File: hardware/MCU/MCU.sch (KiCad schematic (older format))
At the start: 4 parts

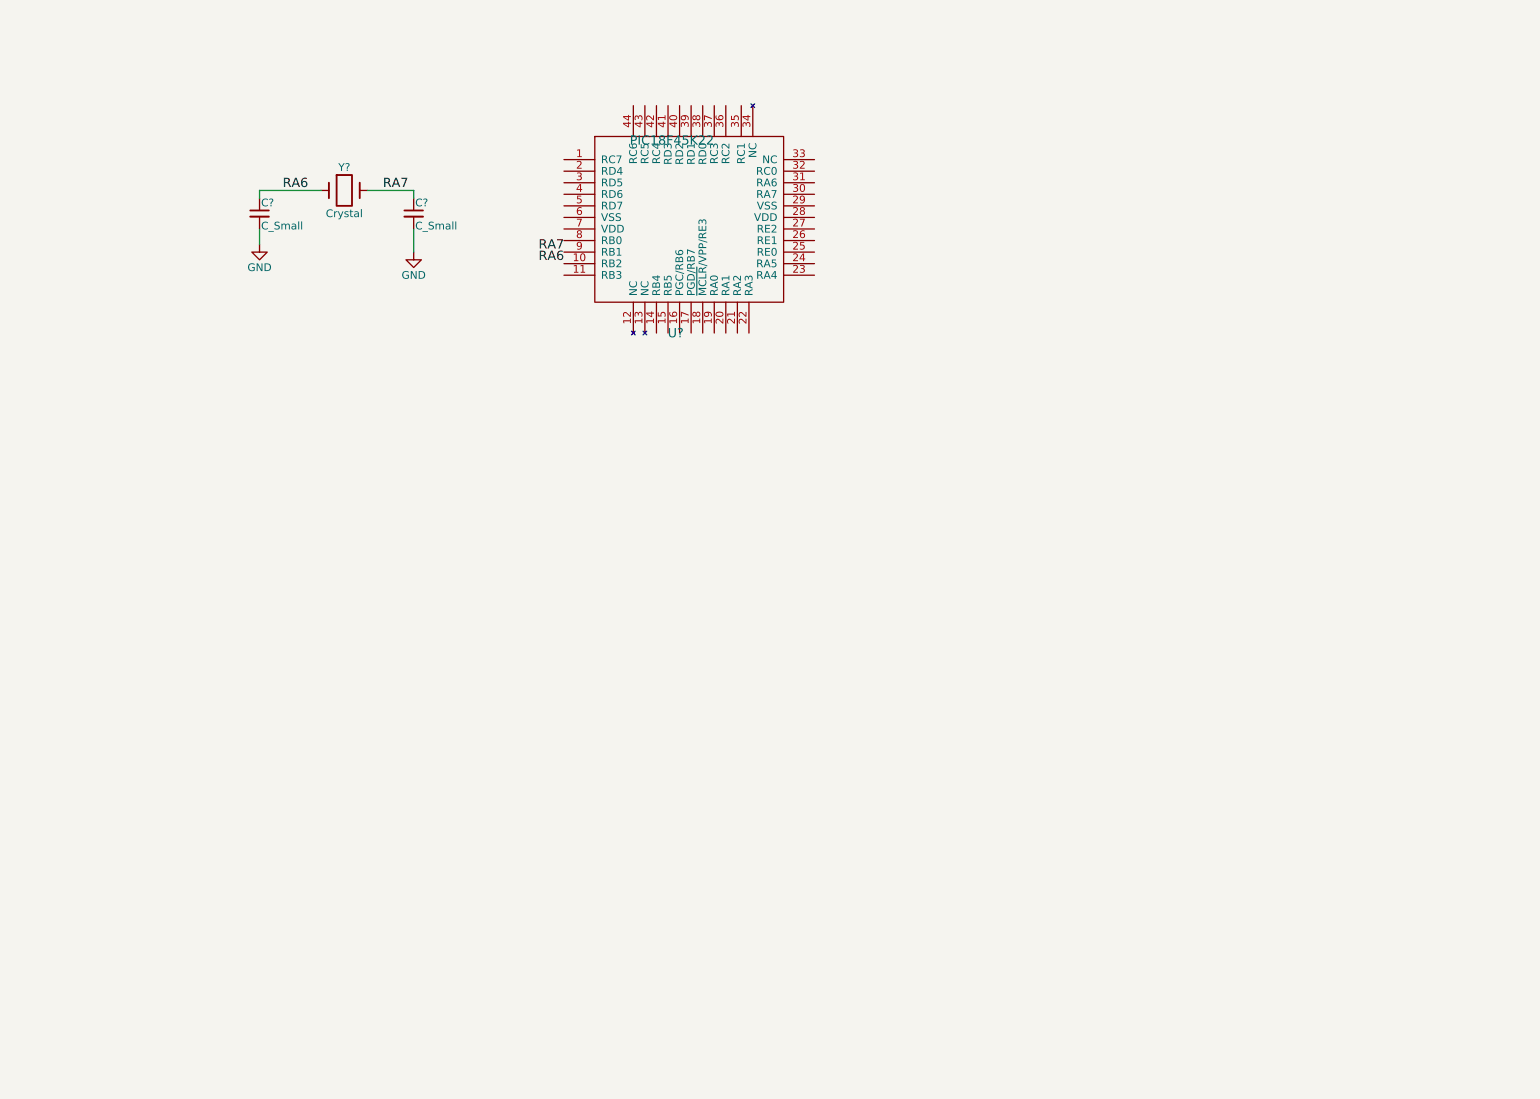
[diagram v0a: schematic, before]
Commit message: MCU: Connectors, watchdog, buzzer added
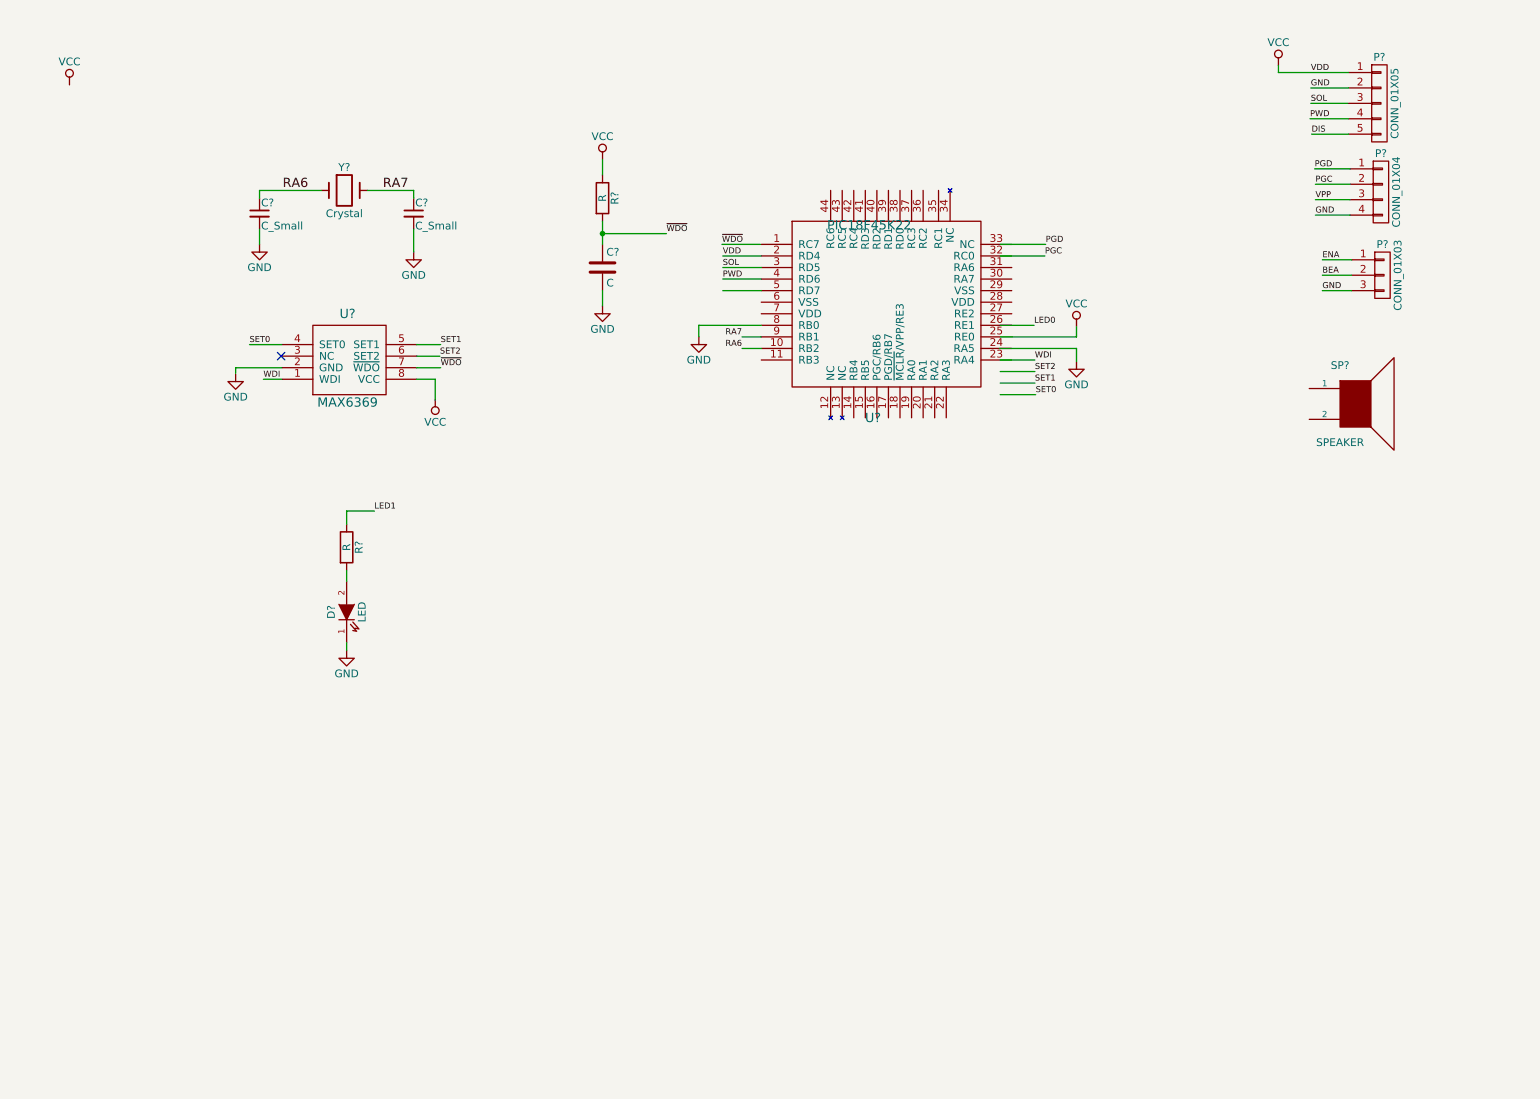
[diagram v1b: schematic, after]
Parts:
- added C?: C, symbol C
- added D?: LED, symbol LED
- added P?: CONN_01X04, symbol CONN_01X04
- added P?: CONN_01X03, symbol CONN_01X03
- added P?: CONN_01X05, symbol CONN_01X05
- added R? (x2): R, symbol R
- added SP?: SPEAKER, symbol SPEAKER
- added U?: MAX6369, symbol MAX6369
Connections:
- net labels added: BEA, DIS, ENA, LED0, LED1, PGC, PGD, PWD, SET0, SET1, SET2, SOL, VCC, VDD, VPP, WDI, ~WDO
- wire segments 6 -> 56
- no-connect marks 0 -> 1
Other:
- moved on the sheet: U?

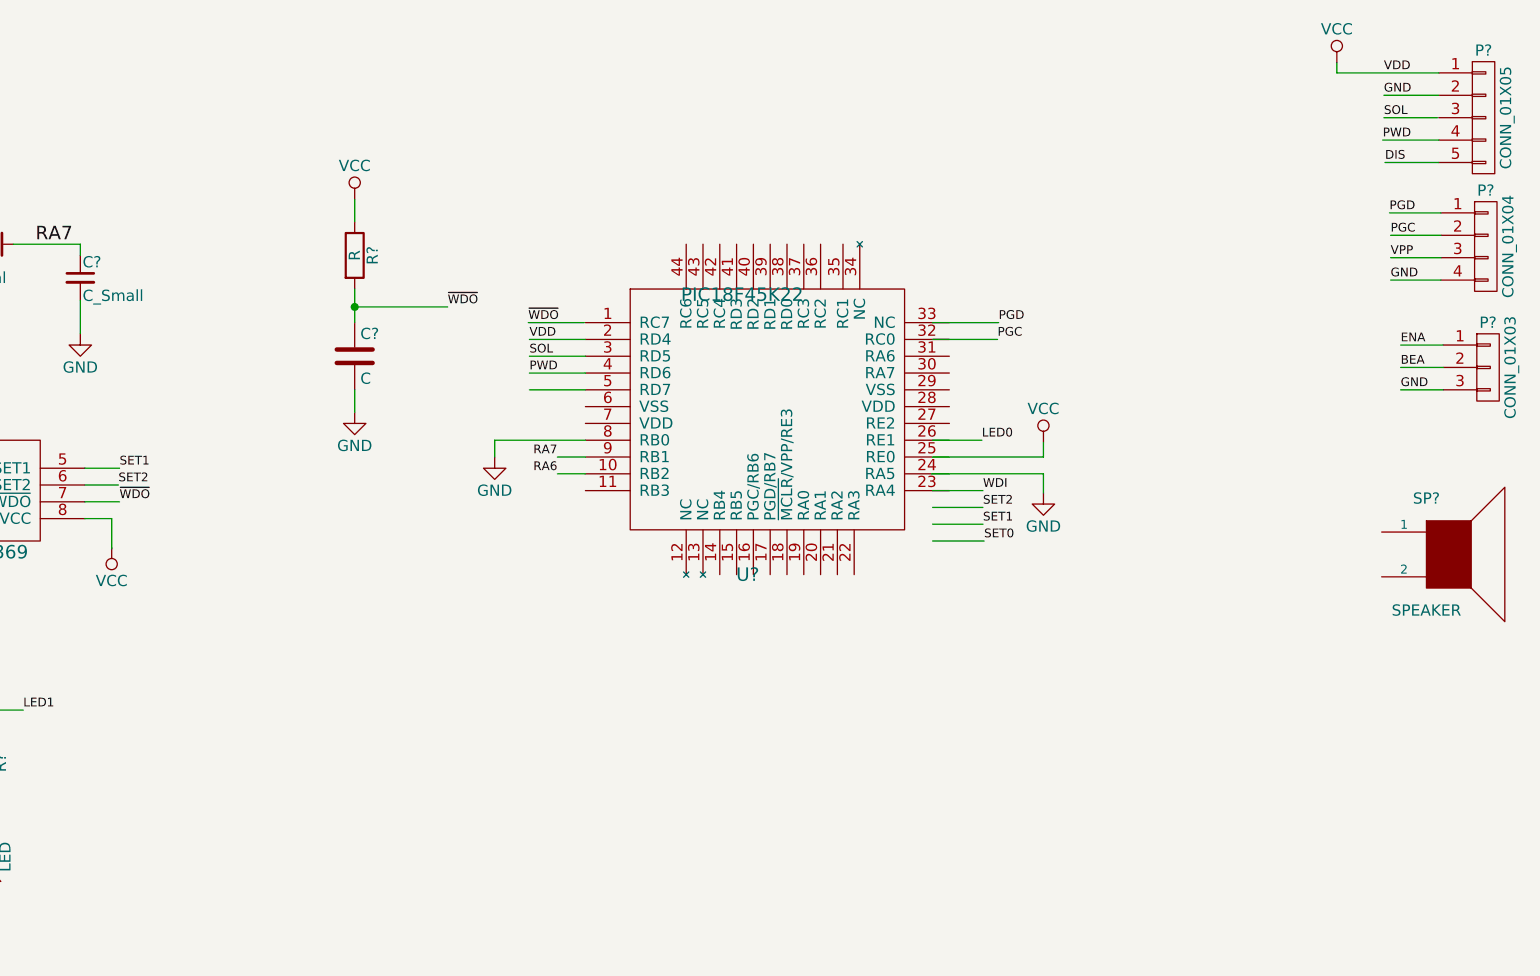
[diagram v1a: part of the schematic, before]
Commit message: LTSpice simulation for 1KHZ Low Pass Filter. Need to adjust with commercial values for passive components
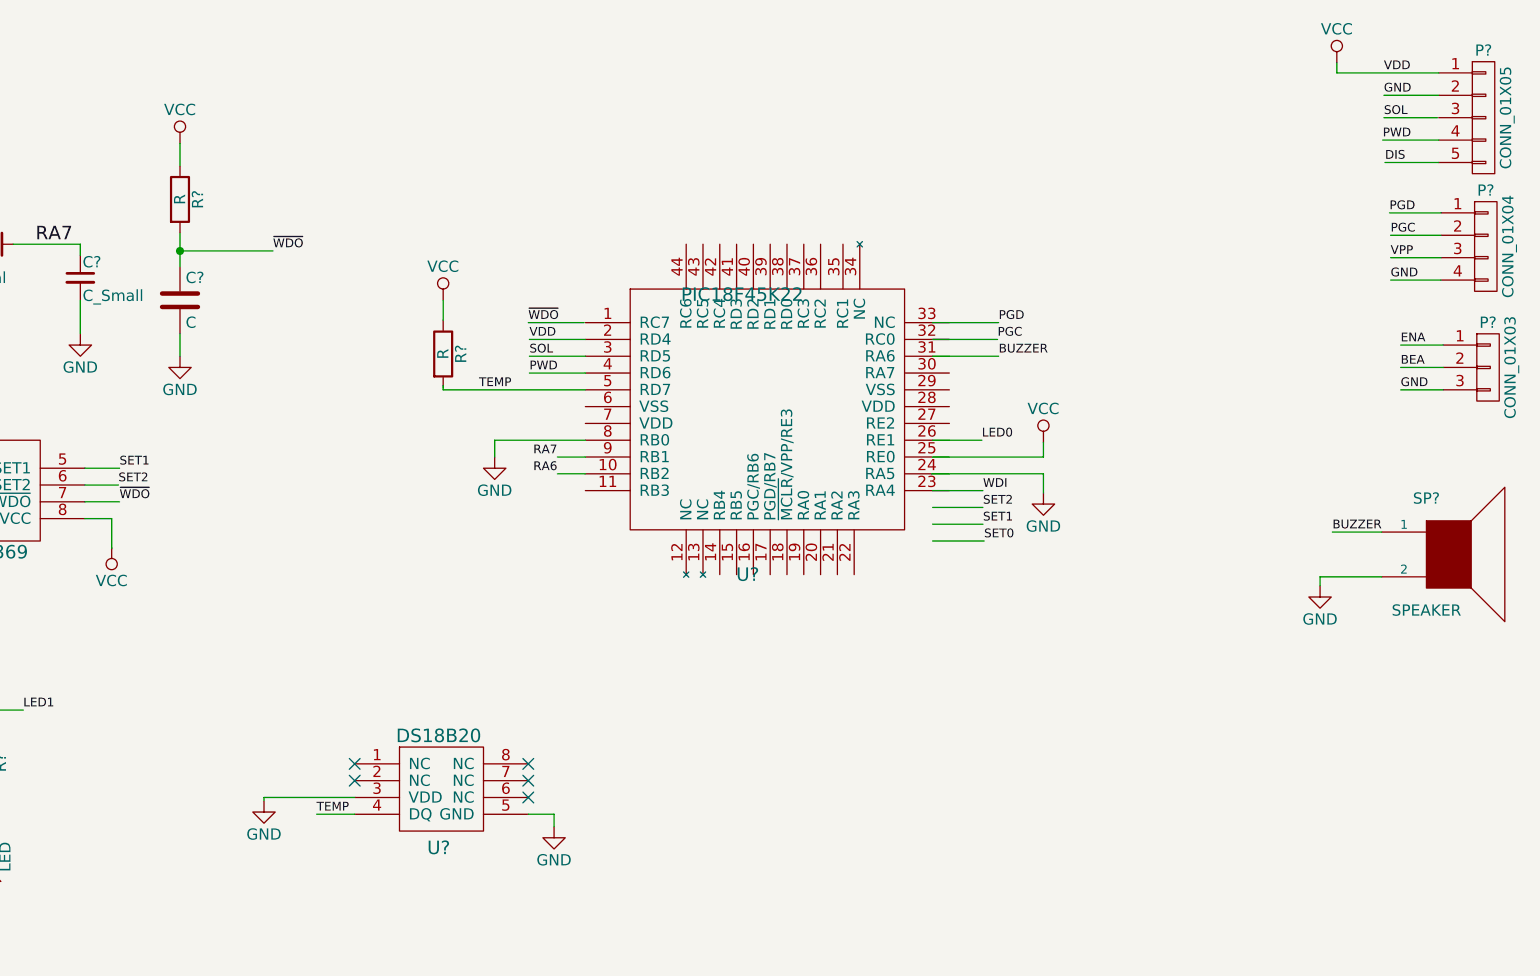
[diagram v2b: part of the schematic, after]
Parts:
- added R?: R, symbol R
- added U?: DS18B20, symbol DS18B20
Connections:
- net labels added: BUZZER, TEMP
- wire segments 56 -> 67
- no-connect marks 1 -> 6
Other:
- moved on the sheet: C?, R?
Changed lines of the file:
@@
 L C C?
 U 1 1 58275BC2
-P 4575 2250
-F 0 "C?" H 4600 2350 50  0000 L CNN
-F 1 "C" H 4600 2150 50  0000 L CNN
-F 2 "" H 4613 2100 50  0000 C CNN
-F 3 "" H 4575 2250 50  0000 C CNN
-	1    4575 2250
+P 3795 2000
+F 0 "C?" H 3820 2100 50  0000 L CNN
+F 1 "C" H 3820 1900 50  0000 L CNN
+F 2 "" H 3833 1850 50  0000 C CNN
+F 3 "" H 3795 2000 50  0000 C CNN
+	1    3795 2000
 	1    0    0    -1
 $EndComp
@@
 L R R?
 U 1 1 58275C23
-P 4575 1800
-F 0 "R?" V 4655 1800 50  0000 C CNN
-F 1 "R" V 4575 1800 50  0000 C CNN
-F 2 "" V 4505 1800 50  0000 C CNN
-F 3 "" H 4575 1800 50  0000 C CNN
-	1    4575 1800
+P 3795 1550
+F 0 "R?" V 3875 1550 50  0000 C CNN
+F 1 "R" V 3795 1550 50  0000 C CNN
+F 2 "" V 3725 1550 50  0000 C CNN
+F 3 "" H 3795 1550 50  0000 C CNN
+	1    3795 1550
 	1    0    0    -1
 $EndComp
@@
 L VCC #PWR?
 U 1 1 58275C66
-P 4575 1550
-F 0 "#PWR?" H 4575 1400 50  0001 C CNN
-F 1 "VCC" H 4575 1700 50  0000 C CNN
-F 2 "" H 4575 1550 50  0000 C CNN
-F 3 "" H 4575 1550 50  0000 C CNN
-	1    4575 1550
+P 3795 1300
+F 0 "#PWR?" H 3795 1150 50  0001 C CNN
+F 1 "VCC" H 3795 1450 50  0000 C CNN
+F 2 "" H 3795 1300 50  0000 C CNN
+F 3 "" H 3795 1300 50  0000 C CNN
+	1    3795 1300
 	1    0    0    -1
 $EndComp
@@
 L GND #PWR?
 U 1 1 58275E7A
-P 4575 2500
-F 0 "#PWR?" H 4575 2250 50  0001 C CNN
-F 1 "GND" H 4575 2350 50  0000 C CNN
-F 2 "" H 4575 2500 50  0000 C CNN
-F 3 "" H 4575 2500 50  0000 C CNN
-	1    4575 2500
+P 3795 2250
+F 0 "#PWR?" H 3795 2000 50  0001 C CNN
+F 1 "GND" H 3795 2100 50  0000 C CNN
+F 2 "" H 3795 2250 50  0000 C CNN
+F 3 "" H 3795 2250 50  0000 C CNN
+	1    3795 2250
 	1    0    0    -1
 $EndComp
 Text Label 5480 2775 2    39   ~ 0
 RA6
-Text Label 4990 2030 0    39   ~ 0
+Text Label 4210 1780 0    39   ~ 0
 ~WDO
 Text Label 5350 2100 0    39   ~ 0
@@
 	1    0    0    -1
 $EndComp
-Wire Wire Line
-	3050 1750 3350 1750
-Wire Wire Line
-	3350 1750 3350 1800
-Wire Wire Line
-	2750 1750 2350 1750
-Wire Wire Line
-	2350 1750 2350 1800
-Wire Wire Line
-	2350 2100 2350 2000
-Wire Wire Line
-	3350 2150 3350 2000
-Wire Wire Line
-	5605 2175 5355 2175
-Wire Wire Line
-	5605 2250 5355 2250
-Wire Wire Line
-	5605 2325 5355 2325
-Wire Wire Line
-	5605 2400 5355 2400
-Wire Wire Line
-	2195 2935 2195 2900
-Wire Wire Line
-	2195 2900 2495 2900
-Wire Wire Line
-	3370 2975 3490 2975
-Wire Wire Line
-	3490 2975 3490 3110
-Wire Wire Line
-	3370 2900 3525 2900
-Wire Wire Line
-	3370 2825 3520 2825
-Wire Wire Line
-	3370 2750 3525 2750
-Wire Wire Line
-	2495 2750 2285 2750
-Wire Wire Line
-	2495 2975 2375 2975
-Wire Wire Line
-	7155 3075 7385 3075
-Wire Wire Line
-	7155 3000 7380 3000
-Wire Wire Line
-	7155 2925 7380 2925
-Wire Wire Line
-	4575 1650 4575 1550
-Wire Wire Line
-	4575 2100 4575 1950
-Wire Wire Line
-	4575 2500 4575 2400
-Wire Wire Line
-	5600 2100 5350 2100
-Wire Wire Line
-	5605 2700 5480 2700
-Wire Wire Line
-	5605 2775 5480 2775
-Wire Wire Line
-	4580 2030 4990 2030
-Connection ~ 4575 2030
-Wire Wire Line
-	7155 2850 7380 2850
-Wire Wire Line
-	2915 4285 2915 4215
-Wire Wire Line
-	2915 4685 2915 4735
-Wire Wire Line
-	2915 3915 2915 3830
-Wire Wire Line
-	2915 3830 3095 3830
-Wire Wire Line
-	7155 2625 7375 2625
-Wire Wire Line
-	7155 2700 7650 2700
-Wire Wire Line
-	7650 2700 7650 2635
-Wire Wire Line
-	7150 2775 7650 2775
-Wire Wire Line
-	7650 2775 7650 2860
-Wire Wire Line
-	5605 2625 5200 2625
-Wire Wire Line
-	5200 2625 5200 2700
-Wire Wire Line
-	7155 2100 7450 2100
-Wire Wire Line
-	7155 2175 7445 2175
-Wire Wire Line
-	9425 1610 9195 1610
-Wire Wire Line
-	9425 1710 9200 1710
-Wire Wire Line
-	9425 1810 9200 1810
-Wire Wire Line
-	9425 1910 9200 1910
 Text Label 9195 1610 0    39   ~ 0
 PGD
@@
 	1    0    0    -1
 $EndComp
-Wire Wire Line
-	9435 2200 9245 2200
-Wire Wire Line
-	9435 2300 9245 2300
-Wire Wire Line
-	9435 2400 9245 2400
 Text Label 9245 2200 0    39   ~ 0
 ENA
@@
 	1    0    0    -1
 $EndComp
-Wire Wire Line
-	9415 1085 9170 1085
-Wire Wire Line
-	9410 1185 9170 1185
-Wire Wire Line
-	9415 1285 9165 1285
-Wire Wire Line
-	9415 1385 9175 1385
 Text Label 9170 985  0    39   ~ 0
 VDD
@@
 	1    0    0    -1
 $EndComp
+$Comp
+L DS18B20 U?
+U 1 1 58276865
+P 4950 4370
+F 0 "U?" H 4950 4295 60  0000 C CNN
+F 1 "DS18B20" H 4950 4795 60  0000 C CNN
+F 2 "" H 4950 4370 60  0001 C CNN
+F 3 "" H 4950 4370 60  0001 C CNN
+	1    4950 4370
+	1    0    0    -1
+$EndComp
+NoConn ~ 4575 4070
+NoConn ~ 4575 4145
+NoConn ~ 5350 4070
+NoConn ~ 5350 4145
+NoConn ~ 5350 4220
+$Comp
+L GND #PWR?
+U 1 1 5827C4C9
+P 5465 4350
+F 0 "#PWR?" H 5465 4100 50  0001 C CNN
+F 1 "GND" H 5465 4200 50  0000 C CNN
+F 2 "" H 5465 4350 50  0000 C CNN
+F 3 "" H 5465 4350 50  0000 C CNN
+	1    5465 4350
+	1    0    0    -1
+$EndComp
+$Comp
+L GND #PWR?
+U 1 1 5827C571
+P 4170 4235
+F 0 "#PWR?" H 4170 3985 50  0001 C CNN
+F 1 "GND" H 4170 4085 50  0000 C CNN
+F 2 "" H 4170 4235 50  0000 C CNN
+F 3 "" H 4170 4235 50  0000 C CNN
+	1    4170 4235
+	1    0    0    -1
+$EndComp
+Text Label 4405 4295 0    39   ~ 0
+TEMP
+$Comp
+L R R?
+U 1 1 5827CEF1
+P 4970 2240
+F 0 "R?" V 5050 2240 50  0000 C CNN
+F 1 "R" V 4970 2240 50  0000 C CNN
+F 2 "" V 4900 2240 50  0000 C CNN
+F 3 "" H 4970 2240 50  0000 C CNN
+	1    4970 2240
+	1    0    0    -1
+$EndComp
+$Comp
+L VCC #PWR?
+U 1 1 5827D694
+P 4970 2000
+F 0 "#PWR?" H 4970 1850 50  0001 C CNN
+F 1 "VCC" H 4970 2150 50  0000 C CNN
+F 2 "" H 4970 2000 50  0000 C CNN
+F 3 "" H 4970 2000 50  0000 C CNN
+	1    4970 2000
+	1    0    0    -1
+$EndComp
+Text Label 5130 2400 0    39   ~ 0
+TEMP
+Text Label 7450 2250 0    39   ~ 0
+BUZZER
+Text Label 8940 3035 0    39   ~ 0
+BUZZER
+$Comp
+L GND #PWR?
+U 1 1 5827E8B2
+P 8885 3275
+F 0 "#PWR?" H 8885 3025 50  0001 C CNN
+F 1 "GND" H 8885 3125 50  0000 C CNN
+F 2 "" H 8885 3275 50  0000 C CNN
+F 3 "" H 8885 3275 50  0000 C CNN
+	1    8885 3275
+	1    0    0    -1
+$EndComp
+Wire Wire Line
+	3050 1750 3350 1750
+Wire Wire Line
+	3350 1750 3350 1800
+Wire Wire Line
+	2750 1750 2350 1750
+Wire Wire Line
+	2350 1750 2350 1800
+Wire Wire Line
+	2350 2100 2350 2000
+Wire Wire Line
+	3350 2150 3350 2000
+Wire Wire Line
+	5605 2175 5355 2175
+Wire Wire Line
+	5605 2250 5355 2250
+Wire Wire Line
+	5605 2325 5355 2325
+Wire Wire Line
+	4970 2400 5605 2400
+Wire Wire Line
+	2195 2935 2195 2900
+Wire Wire Line
+	2195 2900 2495 2900
+Wire Wire Line
+	3370 2975 3490 2975
+Wire Wire Line
+	3490 2975 3490 3110
+Wire Wire Line
+	3370 2900 3525 2900
+Wire Wire Line
+	3370 2825 3520 2825
+Wire Wire Line
+	3370 2750 3525 2750
+Wire Wire Line
+	2495 2750 2285 2750
+Wire Wire Line
+	2495 2975 2375 2975
+Wire Wire Line
+	7155 3075 7385 3075
+Wire Wire Line
+	7155 3000 7380 3000
+Wire Wire Line
+	7155 2925 7380 2925
+Wire Wire Line
+	3795 1400 3795 1300
+Wire Wire Line
+	3795 1850 3795 1700
+Wire Wire Line
+	3795 2250 3795 2150
+Wire Wire Line
+	5600 2100 5350 2100
+Wire Wire Line
+	5605 2700 5480 2700
+Wire Wire Line
+	5605 2775 5480 2775
+Wire Wire Line
+	3800 1780 4210 1780
+Connection ~ 3795 1780
+Wire Wire Line
+	7155 2850 7380 2850
+Wire Wire Line
+	2915 4285 2915 4215
+Wire Wire Line
+	2915 4685 2915 4735
+Wire Wire Line
+	2915 3915 2915 3830
+Wire Wire Line
+	2915 3830 3095 3830
+Wire Wire Line
+	7155 2625 7375 2625
+Wire Wire Line
+	7155 2700 7650 2700
+Wire Wire Line
+	7650 2700 7650 2635
+Wire Wire Line
+	7150 2775 7650 2775
+Wire Wire Line
+	7650 2775 7650 2860
+Wire Wire Line
+	5605 2625 5200 2625
+Wire Wire Line
+	5200 2625 5200 2700
+Wire Wire Line
+	7155 2100 7450 2100
+Wire Wire Line
+	7155 2175 7445 2175
+Wire Wire Line
+	9425 1610 9195 1610
+Wire Wire Line
+	9425 1710 9200 1710
+Wire Wire Line
+	9425 1810 9200 1810
+Wire Wire Line
+	9425 1910 9200 1910
+Wire Wire Line
+	9435 2200 9245 2200
+Wire Wire Line
+	9435 2300 9245 2300
+Wire Wire Line
+	9435 2400 9245 2400
+Wire Wire Line
+	9415 1085 9170 1085
+Wire Wire Line
+	9410 1185 9170 1185
+Wire Wire Line
+	9415 1285 9165 1285
+Wire Wire Line
+	9415 1385 9175 1385
 Wire Wire Line
 	8960 940  8960 985
 Wire Wire Line
 	8960 985  9415 985
+Wire Wire Line
+	5350 4295 5465 4295
+Wire Wire Line
+	5465 4295 5465 4350
+Wire Wire Line
+	4170 4235 4170 4220
+Wire Wire Line
+	4170 4220 4575 4220
+Wire Wire Line
+	4575 4295 4405 4295
+Wire Wire Line
+	4970 2400 4970 2380
+Wire Wire Line
+	4970 2000 4970 2090
+Wire Wire Line
+	7155 2250 7450 2250
+Wire Wire Line
+	9160 3035 8940 3035
+Wire Wire Line
+	9160 3235 8885 3235
+Wire Wire Line
+	8885 3235 8885 3275
 $EndSCHEMATC

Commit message: MCU schematic: Low Pass Filter for BEA signal. DRC cheched and Netlist generated
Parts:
- added C4, C5, C6: 10nF, symbol C
- added R4: 6,19K, symbol R
- added R5: 4,99K, symbol R
- added R6: 6,65K, symbol R
- added U4: OP275, symbol OP275
- gave numbers to parts that had none: 15
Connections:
- net labels added: F_BEA
- net labels removed: LED1
- wire segments 67 -> 96
- no-connect marks 6 -> 13
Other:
- moved on the sheet: U1, U2
